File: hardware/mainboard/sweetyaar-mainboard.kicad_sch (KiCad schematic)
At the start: 79 parts

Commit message: WIP led changes
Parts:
- removed LED1: RGB_LED_5MM, symbol Device:LED_KRGB
- removed R_LED_B1, R_LED_G1, R_LED_R1: 330, symbol Device:R
- added C_LED1: 100n, symbol Device:C
- added D_LED1: WS2812B, LED_THT:LED_D5.0mm-4_RGB, symbol SweetYaar:WS2812B
- added Q_LED1: MMBT3904, Package_TO_SOT_SMD:SOT-23, symbol Transistor_BJT:MMBT3904
- added R_LED_BASE1: 10k, symbol Device:R
- added R_LED_PULLUP1: 4.7k, symbol Device:R
- added TP1, TP2, TP3: TestPoint, symbol Connector:TestPoint
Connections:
- net 5V_PERIPH_SW: now also C_LED1.1, D_LED1.2 (VDD), R_LED_PULLUP1.1, TP1.1
- net GND: now also C_LED1.2, D_LED1.3 (VSS), Q_LED1.2 (E), TP3.1
- net LED_BLUE: no longer names the net of U_ESP32.28 (IO17)
- net LED_GREEN: no longer names the net of U_ESP32.27 (IO16)
- net LED_RED renamed STATUS_LED_GPIO
- net STATUS_LED_GPIO: now also R_LED_BASE1.2
- new net: D_LED1.4 (DIN), Q_LED1.3 (C), R_LED_PULLUP1.2
- new net: D_LED1.1 (DOUT), TP2.1
- new net: Q_LED1.1 (B), R_LED_BASE1.1
- no-connect marks 28 -> 30
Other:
- note added: "Test points to allow easy connection of later added additional LEDs."

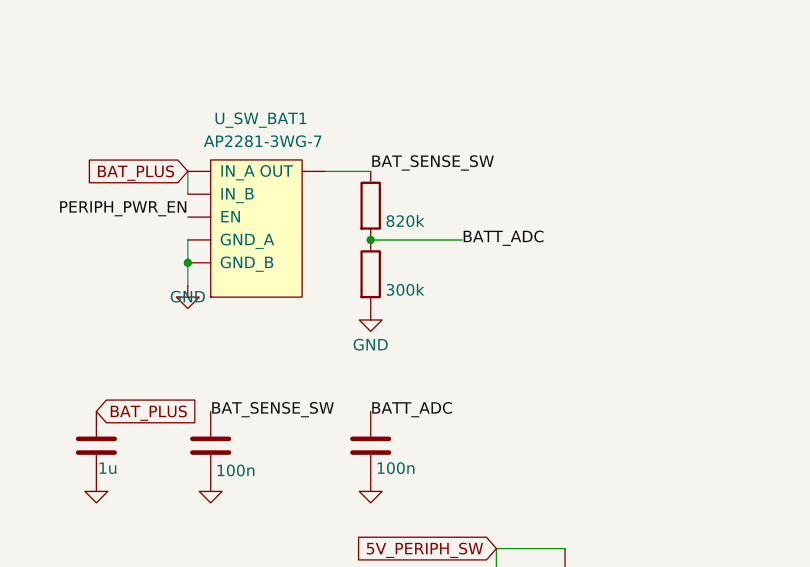
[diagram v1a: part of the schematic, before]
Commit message: Update battery divider and ADC diagnostics
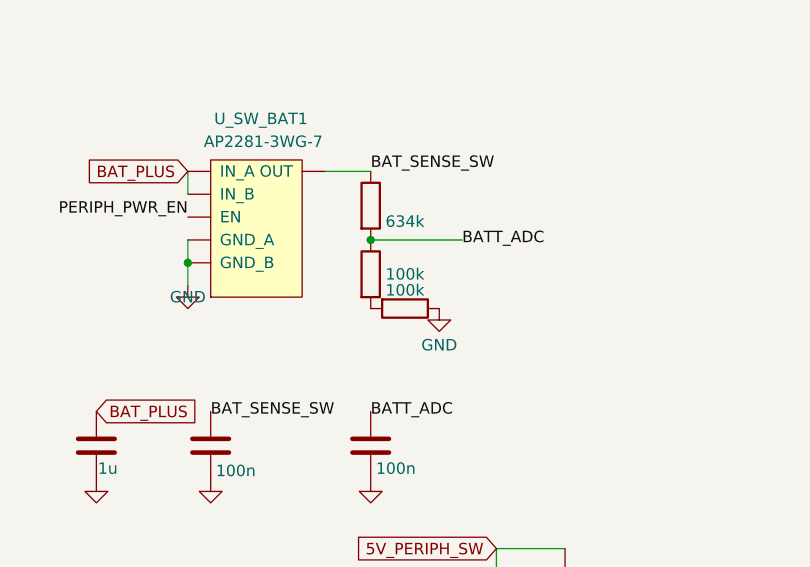
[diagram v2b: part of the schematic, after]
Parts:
- added R_BAT_L2: 100k, symbol Device:R
- R_BAT_H1: value 820k -> 634k
- R_BAT_L1: value 300k -> 100k
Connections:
- net GND: now also R_BAT_L2.1; no longer R_BAT_L1.2
- new net: R_BAT_L1.2, R_BAT_L2.2
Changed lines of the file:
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@@
 			)
 		)
-		(property "Value" "820k"
+		(property "Value" "634k"
 			(at 345.438 173.21 0)
 			(show_name no)
@@
 			)
 		)
-		(property "Value" "300k"
+		(property "Value" "100k"
 			(at 345.44 180.848 0)
 			(show_name no)
@@
 	(symbol
 		(lib_id "power:GND")
-		(at 341.63 182.88 0)
+		(at 349.25 182.88 0)
 		(unit 1)
 		(body_style 1)
@@
 		(dnp no)
 		(property "Reference" "#PWR041"
-			(at 341.63 182.88 0)
+			(at 349.25 182.88 0)
 			(hide yes)
 			(show_name no)
@@
 		)
 		(property "Value" "GND"
-			(at 341.63 186.944 0)
-			(show_name no)
-			(do_not_autoplace no)
-			(effects
-				(font
-					(size 1.27 1.27)
-				)
-			)
-		)
-		(property "Footprint" ""
-			(at 341.63 182.88 0)
-			(show_name no)
-			(do_not_autoplace no)
-			(effects
-				(font
-					(size 1.27 1.27)
-				)
-			)
-		)
-		(property "Datasheet" ""
-			(at 341.63 182.88 0)
-			(show_name no)
-			(do_not_autoplace no)
-			(effects
-				(font
-					(size 1.27 1.27)
-				)
-			)
-		)
-		(property "Description" ""
-			(at 341.63 182.88 0)
+			(at 349.25 186.944 0)
+			(show_name no)
+			(do_not_autoplace no)
+			(effects
+				(font
+					(size 1.27 1.27)
+				)
+			)
+		)
+		(property "Footprint" ""
+			(at 349.25 182.88 0)
+			(show_name no)
+			(do_not_autoplace no)
+			(effects
+				(font
+					(size 1.27 1.27)
+				)
+			)
+		)
+		(property "Datasheet" ""
+			(at 349.25 182.88 0)
+			(show_name no)
+			(do_not_autoplace no)
+			(effects
+				(font
+					(size 1.27 1.27)
+				)
+			)
+		)
+		(property "Description" ""
+			(at 349.25 182.88 0)
 			(show_name no)
 			(do_not_autoplace no)
@@
 					(unit 1)
 				)
+			)
+		)
+	)
+	(symbol
+		(lib_id "Device:R")
+		(at 345.44 182.88 270)
+		(unit 1)
+		(body_style 1)
+		(exclude_from_sim no)
+		(in_bom yes)
+		(on_board yes)
+		(in_pos_files yes)
+		(dnp no)
+		(property "Reference" "R_BAT_L2"
+			(at 347.98 184.15 0)
+			(hide yes)
+			(show_name no)
+			(do_not_autoplace no)
+			(effects
+				(font
+					(size 1.27 1.27)
+				)
+			)
+		)
+		(property "Value" "100k"
+			(at 345.44 179.07 90)
+			(show_name no)
+			(do_not_autoplace no)
+			(effects
+				(font
+					(size 1.27 1.27)
+				)
+			)
+		)
+		(property "Footprint" ""
+			(at 345.44 182.88 0)
+			(hide yes)
+			(show_name no)
+			(do_not_autoplace no)
+			(effects
+				(font
+					(size 1.27 1.27)
+				)
+			)
+		)
+		(property "Datasheet" ""
+			(at 345.44 182.88 0)
+			(hide yes)
+			(show_name no)
+			(do_not_autoplace no)
+			(effects
+				(font
+					(size 1.27 1.27)
+				)
+			)
+		)
+		(property "Description" ""
+			(at 345.44 182.88 0)
+			(show_name no)
+			(do_not_autoplace no)
+			(effects
+				(font
+					(size 1.27 1.27)
+				)
+			)
+		)
+		(pin "1"
+		)
+		(pin "2"
+		)
+		(instances
+			(project "sweetyaar-mainboard"
+				(path "/a2bc0001-0000-4000-8000-000000000001"
+					(reference "R_BAT_L2")
+					(unit 1)
+				)

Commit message: Add schematics
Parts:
- removed TP1, TP2, TP3: TestPoint, symbol Connector:TestPoint
- added D2: ESD441, Package_SON:Texas_DPY0002A_0.6x1mm_P0.65mm, symbol Device:D_Zener
- added JP3: SolderJumper_2_Open, Jumper:SolderJumper-2_P1.3mm_Open_RoundedPad1.0x1.5mm, symbol Jumper:SolderJumper_2_Open
- added J_LED_EXT1: Conn_01x03, Connector_JST:JST_XH_B3B-XH-A_1x03_P2.50mm_Vertical, symbol Connector_Generic:Conn_01x03
- added R_TH1: 10k, Resistor_SMD:R_0603_1608Metric, symbol Device:R
- C1: value 100nF -> 100nF, 50 V, X7R, ±10%; footprint (none) -> Capacitor_SMD:C_0603_1608Metric; LCSC (none) -> C14663
- C17, C_3V3_IN1, C_AMP2, C_CHG_SYS1, C_ESP2, C_SD2: value 10u -> 10uF, 25V X5R/X7R, ±20%; footprint (none) -> Capacitor_SMD:C_0805_2012Metric; LCSC (none) -> C15850
- C2, C_5V_OUT1, C_5V_OUT2: value 22u -> 22uF, 16 V, X5R/X7R, ±20%; footprint (none) -> Capacitor_SMD:C_1206_3216Metric; LCSC (none) -> C90146
- C_AMP1, C_BAT_ADC1, C_BAT_SW_OUT1, C_ESP1, C_LED1, C_SD1, C_SD_SW_OUT1: value 100n -> 100nF, 50 V, X7R, ±10%; footprint (none) -> Capacitor_SMD:C_0603_1608Metric; LCSC (none) -> C14663
- C_AMP3: value 470u -> 470uF, 10V 105°C, low-ESR electrolytic; footprint (none) -> Capacitor_THT:CP_Radial_D8.0mm_P3.50mm; LCSC (none) -> C88765
- C_BAT_SW_IN1, C_ESP_EN1, C_MUX1, C_MUX2, C_SD_SW_IN1: value 1u -> 1uF, 25 V, X7R, ±10%; footprint (none) -> Capacitor_SMD:C_0603_1608Metric; LCSC (none) -> C29936
- C_CHG_BAT1, C_MUX3: value 1u -> 2.2 uF, 25 V, X7R, ±10%; footprint (none) -> Capacitor_SMD:C_0805_2012Metric; LCSC (none) -> C126591
- D1: LCSC (none) -> C53161160
- D_LED1: value WS2812B -> WS2812D-F5-12mA-C1; LCSC (none) -> C4154875
- JP1, JP2: footprint (none) -> Jumper:SolderJumper-2_P1.3mm_Open_RoundedPad1.0x1.5mm; LCSC (none) -> N/A
- JP_ILIM1, JP_ISET1: footprint (none) -> Jumper:SolderJumper-2_P1.3mm_Bridged_RoundedPad1.0x1.5mm; LCSC (none) -> N/A; now left out of the parts list
- J_AUX1, J_SPEAKER1, J_SWITCH1: footprint (none) -> Connector_JST:JST_XH_B2B-XH-A_1x02_P2.50mm_Vertical; LCSC (none) -> C158012; now not fitted
- J_BATT1: footprint (none) -> Connector_JST:JST_XH_B3B-XH-A_1x03_P2.50mm_Vertical; LCSC (none) -> C144394; now not fitted
- J_BTN1: footprint (none) -> Connector_JST:JST_XH_B4B-XH-A_1x04_P2.50mm_Vertical; LCSC (none) -> C144395; now not fitted
- J_PROG1: footprint (none) -> SweetYaar:DebuggerPad_1x06_P2.54mm; LCSC (none) -> N/A; now left out of the parts list
- J_USB1: footprint (none) -> Connector_USB:USB_C_Receptacle_Molex_105450-0101; LCSC (none) -> C134092
- L_3V3, L_5V1: footprint (none) -> SweetYaar:L_Murata_DFE201612E; LCSC (none) -> C668312
- Q_LED1: LCSC (none) -> C20526
- R_3V3_BOT1, R_5V_BOT1: footprint (none) -> Resistor_SMD:R_0603_1608Metric; LCSC (none) -> C23265
- R_3V3_TOP1: footprint (none) -> Resistor_SMD:R_0603_1608Metric; LCSC (none) -> C23192
- R_5V_EN_PD1, R_BAT_L1, R_BAT_L2, R_PR1_BOT1: footprint (none) -> Resistor_SMD:R_0603_1608Metric; LCSC (none) -> C25803
- R_5V_TOP1: footprint (none) -> Resistor_SMD:R_0603_1608Metric; LCSC (none) -> C23252
- R_BAT_H1, R_SDMODE1: footprint (none) -> Resistor_SMD:R_0603_1608Metric; LCSC (none) -> C861504
- R_BOOT_PULLUP1, R_ESP_EN_PULLUP1, R_LED_BASE1, R_SD_CS1, R_SD_DAT1, R_SD_DAT2, R_SD_MISO1, R_SD_MOSI1, R_STAT1, R_STAT2: footprint (none) -> Resistor_SMD:R_0603_1608Metric; LCSC (none) -> C25804
- R_CC1, R_CC2, R_ILIM1: footprint (none) -> Resistor_SMD:R_0603_1608Metric; LCSC (none) -> C23186
- R_ILIM2: footprint (none) -> Resistor_SMD:R_0603_1608Metric; LCSC (none) -> C22797
- R_ISET1, R_ISET2: footprint (none) -> Resistor_SMD:R_0603_1608Metric; LCSC (none) -> C25192
- R_LED_PULLUP1: value 4.7k -> 1k; footprint (none) -> Resistor_SMD:R_0603_1608Metric; LCSC (none) -> C21190
- R_PR1_TOP1: footprint (none) -> Resistor_SMD:R_0603_1608Metric; LCSC (none) -> C23024
- R_VIB1: footprint (none) -> Resistor_SMD:R_0603_1608Metric; LCSC (none) -> C23178
- SW_VIB1: footprint (none) -> Resistor_THT:R_Axial_DIN0516_L15.5mm_D5.0mm_P20.32mm_Horizontal; LCSC (none) -> N/A; now not fitted
- TH1: LCSC (none) -> N/A; now not fitted; now left out of the parts list
- U_3V3, U_5V1: LCSC (none) -> C2845237
- U_AMP1: LCSC (none) -> C910544
- U_CHG1: LCSC (none) -> C19725033
- U_ESP32: value ESP32-WROOM-32 -> ESP32-WROOM-32E-N8; footprint (none) -> RF_Module:ESP32-WROOM-32E; symbol RF_Module:ESP32-WROOM-32 -> RF_Module:ESP32-WROOM-32E; LCSC (none) -> C701342
- U_MUX1: value TPS2116DRL -> TPS2116DRLR; footprint (none) -> Package_TO_SOT_SMD:SOT-583-8; LCSC (none) -> C3235557
- U_SW_BAT1, U_SW_SD1: footprint (none) -> Package_TO_SOT_SMD:SOT-23-6; LCSC (none) -> C128634
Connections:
- net 5V_PERIPH_SW: now also J_LED_EXT1.1 (Pin_1)
- net AUX_5V_IN: now also D2.1 (K)
- net BAT_TEMP: now also TH1.2, JP3.2 (B); no longer TH1.1
- net GND: now also TH1.1, U_ESP32.[1,15,38,39] (GND), D2.2 (A), J_LED_EXT1.3 (Pin_3), R_TH1.2; no longer TH1.2, U_ESP32.1 (GND), U_ESP32.15 (GND), U_ESP32.38 (GND), U_ESP32.39 (GND)
- net at D_LED1.1 (DOUT): now also J_LED_EXT1.2 (Pin_2)
- new net: JP3.1 (A), R_TH1.1
- no-connect marks 30 -> 24
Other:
- note added: "If the thermistor is omitted: connect jumper to allow a 10K resistor"
- note removed: "If the thermistor is omitted from the harness - populate with a 10kΩ resistor instead"

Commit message: switching to WS2812B-V6 LED
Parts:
- removed Q_LED1: MMBT3904, Package_TO_SOT_SMD:SOT-23, symbol Transistor_BJT:MMBT3904
- removed R_LED_BASE1: 10k, Resistor_SMD:R_0603_1608Metric, symbol Device:R
- removed R_LED_PULLUP1: 1k, Resistor_SMD:R_0603_1608Metric, symbol Device:R
- added R_LED_DIN1: 301, Resistor_SMD:R_0603_1608Metric, symbol Device:R
- D_LED1: value WS2812D-F5-12mA-C1 -> WS2812B-V6; footprint LED_THT:LED_D5.0mm-4_RGB -> LCSC:WS2812B-V6; symbol SweetYaar:WS2812B -> LCSC:WS2812B-V6; LCSC C4154875 -> C52917433; Manufacturer (none) -> worldsemi; Manufacturer Part (none) -> WS2812B-V6
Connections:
- net 5V_PERIPH_SW: now also D_LED1.1 (VDD); no longer D_LED1.2 (VDD)
- net STATUS_LED_GPIO: now also R_LED_DIN1.2
- net at D_LED1.4 (DIN): now also R_LED_DIN1.1
- net at J_LED_EXT1.2 (Pin_2): now also D_LED1.2 (DOUT); no longer D_LED1.1 (DOUT)

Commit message: changing debugger components to match mainboard
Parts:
- J_USB1: value USB-C -> TYPE-C-31-M-12; footprint Connector_USB:USB_C_Receptacle_Molex_105450-0101 -> Connector_USB:USB_C_Receptacle_HRO_TYPE-C-31-M-12; symbol Connector:USB_C_Receptacle -> Connector:USB_C_Receptacle_USB2.0_16P; LCSC C134092 -> C165948
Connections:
- no-connect marks 24 -> 16
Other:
- moved on the sheet: J_AUX1, J_BTN1, J_PROG1

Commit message: changing 634k resistor part
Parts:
- R_BAT_H1, R_SDMODE1: LCSC C861504 -> C65831
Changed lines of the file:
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@@
 			)
 		)
-		(property "LCSC" "C861504"
+		(property "LCSC" "C65831"
 			(at 341.63 171.45 0)
 			(hide yes)
@@
 			)
 		)
-		(property "LCSC" "C861504"
+		(property "LCSC" "C65831"
 			(at 152.4 269.24 90)
 			(hide yes)

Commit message: Add mainboard PCB placement and shared KiCad assets
Add the initial placement-only mainboard PCB and design rules. Include the shared symbols, footprints, and 3D models used by the board, and stop tracking generated KiCad backup files.
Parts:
- added TP1, TP10, TP11, TP12, TP13, TP14, TP15, TP16, TP2, TP3, TP4, TP5, TP6, TP7, TP8, TP9: ${SHORT_NET_NAME(1)}, TestPoint:TestPoint_Pad_D2.0mm, symbol Connector:TestPoint
- D1, D2: footprint Package_SON:Texas_DPY0002A_0.6x1mm_P0.65mm -> SweetYaar:Texas_DPY0002A_0.6x1mm_P0.65mm
- D_LED1: footprint LCSC:WS2812B-V6 -> SweetYaar:WS2812B-V6
- J_SD1: footprint Connector_Card:microSD_HC_Molex_104031-0811 -> SweetYaar:microSD_HC_Molex_104031-0811; symbol Connector:Micro_SD_Card -> Connector:Micro_SD_Card_Det2
- J_USB1: footprint Connector_USB:USB_C_Receptacle_HRO_TYPE-C-31-M-12 -> SweetYaar:USB_C_Receptacle_HRO_TYPE-C-31-M-12
- U_AMP1: footprint Package_DFN_QFN:TQFN-16-1EP_3x3mm_P0.5mm_EP1.23x1.23mm -> SweetYaar:TQFN-16-1EP_3x3mm_P0.5mm_EP1.23x1.23mm
- U_CHG1: footprint SweetYaar:WSON10_DLH_TEX -> SweetYaar:Texas_DLH0010A_WSON-10-1EP_2.2x2mm_P0.4mm_EP0.9x1.5mm
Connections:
- net 3V3_AON: now also TP8.1
- net 3V3_PERIPH_SW: now also TP7.1
- net 5V_INPUT: now also TP4.1
- net 5V_PERIPH_SW: now also TP6.1
- net AUX_5V_IN: now also TP2.1
- net BATT_ADC: now also TP10.1
- net BAT_PLUS: now also TP3.1
- net BAT_TEMP: now also TP11.1
- net GND: now also TP12.1, TP13.1, TP14.1, TP15.1, TP16.1
- net PERIPH_PWR_EN: now also TP9.1
- net SYS_SW: now also TP5.1
- net USB_VBUS: now also TP1.1
- no-connect marks 16 -> 18
